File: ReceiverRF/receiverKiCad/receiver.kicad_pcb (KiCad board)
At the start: 2 copper layers, 95.4 x 60 mm, 75 parts, among them J1 RF2-03E-T-00-50-G, J2 Conn_01x05_Socket, J3 Conn_01x04, Q1 MMBT3904, SW1 SW_Push, SW2 SW_Push, SW3 SW_Push, SW4 SW_Push, SW5 SW_SPST, U1 STM32F103RET6, U2 NCV5501DT33RKG, U3 NJM2882F05-TE1, U4 MLX90393SLW-ABA-011-RE, Y1 YG8M000000S418

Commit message: changement cristal
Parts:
- Y1: value YG8M000000S418 -> CTX853CT-ND
- moved CSTL_C1 0.93 mm to (145.8, 83.2), turned to 0 degrees
- moved Y1 0.25 mm to (140.0, 84.4), turned to 0 degrees
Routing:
- net OSC_IN: track 10.2 -> 16.2 mm

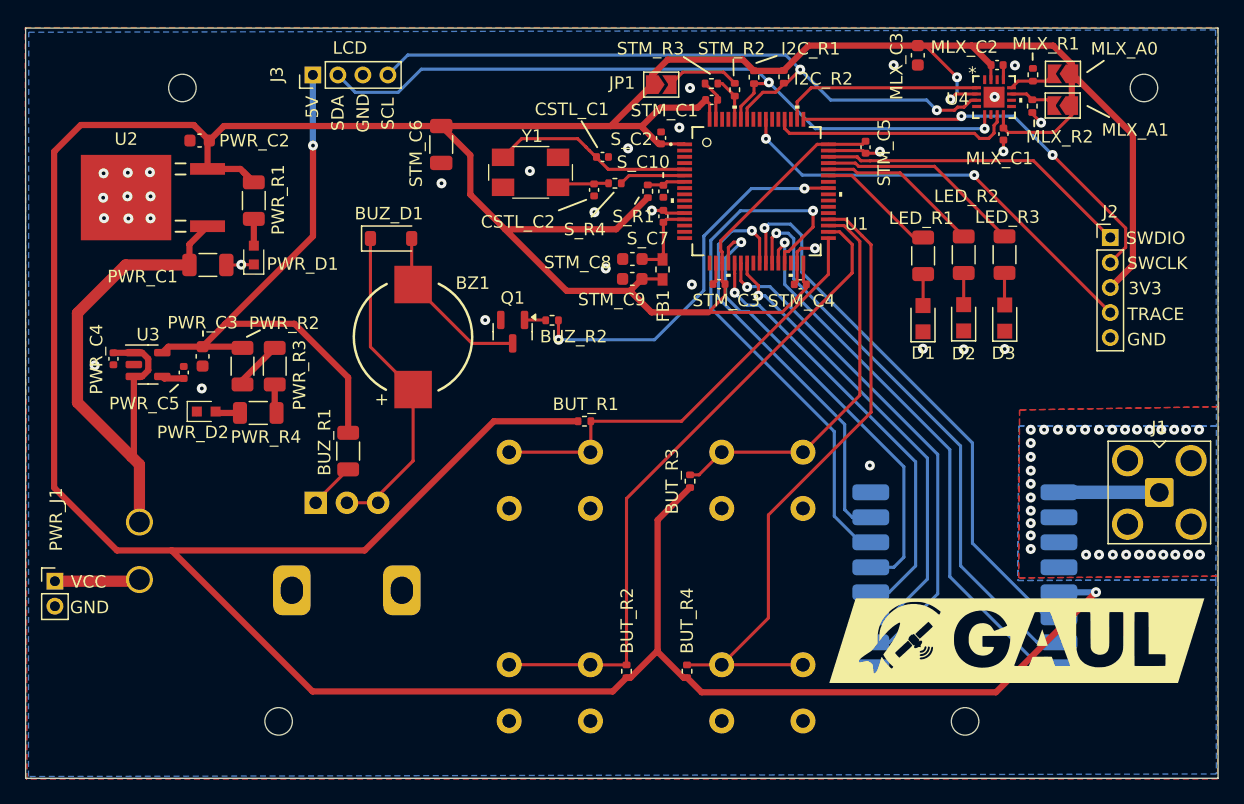
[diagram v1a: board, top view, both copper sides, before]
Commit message: changement vers footprint 1206
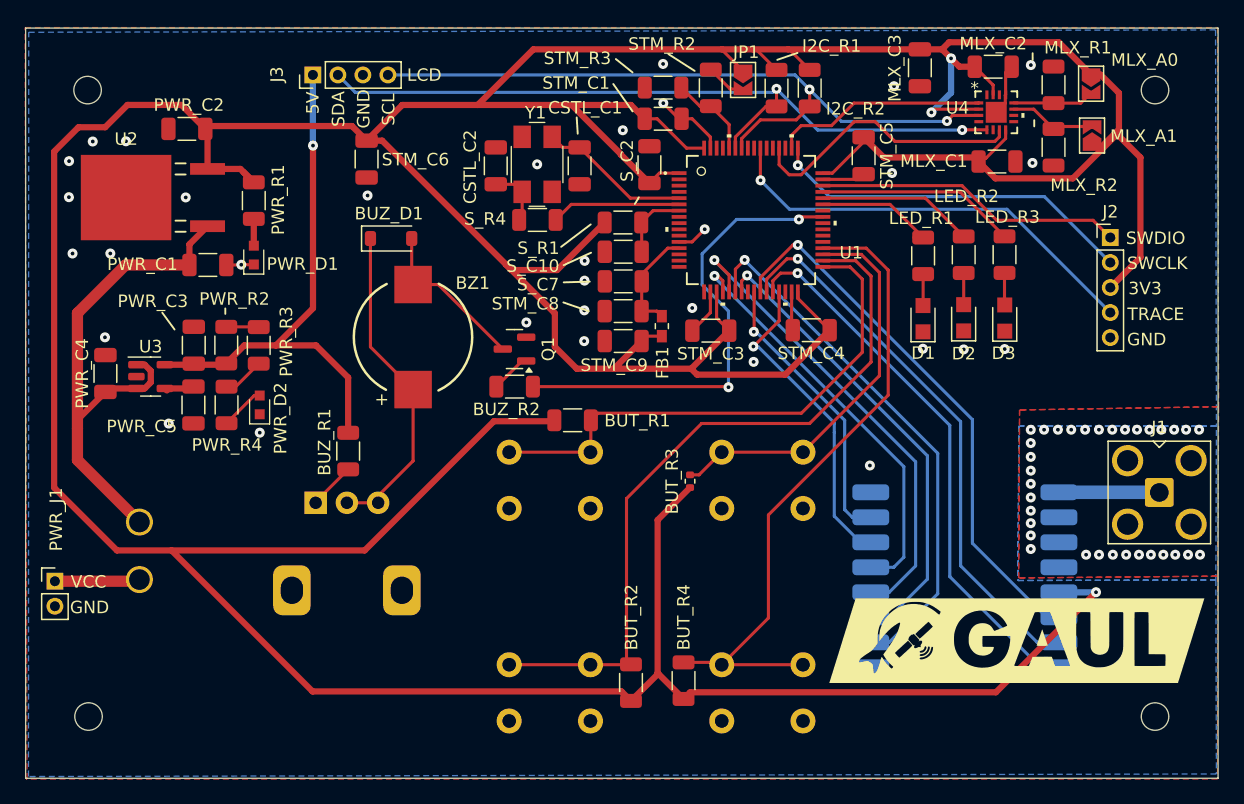
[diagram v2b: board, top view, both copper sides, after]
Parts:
- BUT_R1, BUT_R2, BUT_R4, BUZ_R2, I2C_R1, I2C_R2, MLX_R1, MLX_R2, STM_R2, STM_R3, S_R1, S_R4: footprint Resistor_SMD:R_0402_1005Metric -> Resistor_SMD:R_1206_3216Metric
- CSTL_C1, CSTL_C2, MLX_C1, MLX_C2, PWR_C4, PWR_C5, STM_C1, STM_C3, STM_C4, STM_C5, S_C10, S_C2, S_C7: footprint Capacitor_SMD:C_0402_1005Metric -> Capacitor_SMD:C_1206_3216Metric
- MLX_C3, PWR_C2, PWR_C3, STM_C8, STM_C9: footprint Capacitor_SMD:C_0603_1608Metric -> Capacitor_SMD:C_1206_3216Metric
- moved REF** 15.2 mm to (104.7, 127.9)
- moved REF** 15.2 mm to (190.0, 127.9)
- moved CSTL_C2 8.10 mm to (137.3, 83.9), turned to 90 degrees
- moved REF** 7.59 mm to (104.6, 77.8)
- moved S_R4 6.86 mm to (140.6, 88.2)
- moved JP1 6.55 mm to (157.0, 77.0), turned to -90 degrees
- moved S_C7 6.11 mm to (147.5, 93.1), turned to 180 degrees
- moved BUZ_R2 6.09 mm to (138.8, 101.5)
- moved STM_C6 6.08 mm to (126.9, 83.3)
- moved S_C10 5.80 mm to (147.5, 90.7), turned to 180 degrees
- moved STM_C9 5.02 mm to (147.5, 97.9)
- moved FB1 4.54 mm to (150.5, 96.7)
- moved PWR_D2 4.31 mm to (118.4, 103.0), turned to 90 degrees
- moved STM_C8 4.24 mm to (147.4, 95.5)
- moved STM_C1 4.16 mm to (150.6, 80.1)
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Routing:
- net +3.3V: track 406.6 -> 458.3 mm
- net RFM_NIRQ: track 44.4 -> 25.5 mm
- net RFM_SDN: track 33.7 -> 22.9 mm
- net BUZZER: track 30.8 -> 38.1 mm
- net PUSH_1: track 35.8 -> 42.6 mm
- net PUSH_2: track 52.8 -> 58.4 mm
- net OSC_OUT: track 5.32 -> 10.4 mm
- net +5V: track 48.1 -> 43.7 mm
- net OSC_IN: track 16.2 -> 12.2 mm
- net SPI_RFM_CS: track 37.4 -> 33.5 mm
- net SPI_SCK: track 35.2 -> 38.6 mm
- net BOOT0: track 3.64 -> 6.93 mm
- net SYS_SWCLK: track 32.9 -> 29.6 mm, vias 2 -> 1
- net Net-(MLX_A1-B): track 3.76 -> 7.00 mm
- net Net-(MLX_A0-B): track 3.85 -> 6.85 mm
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
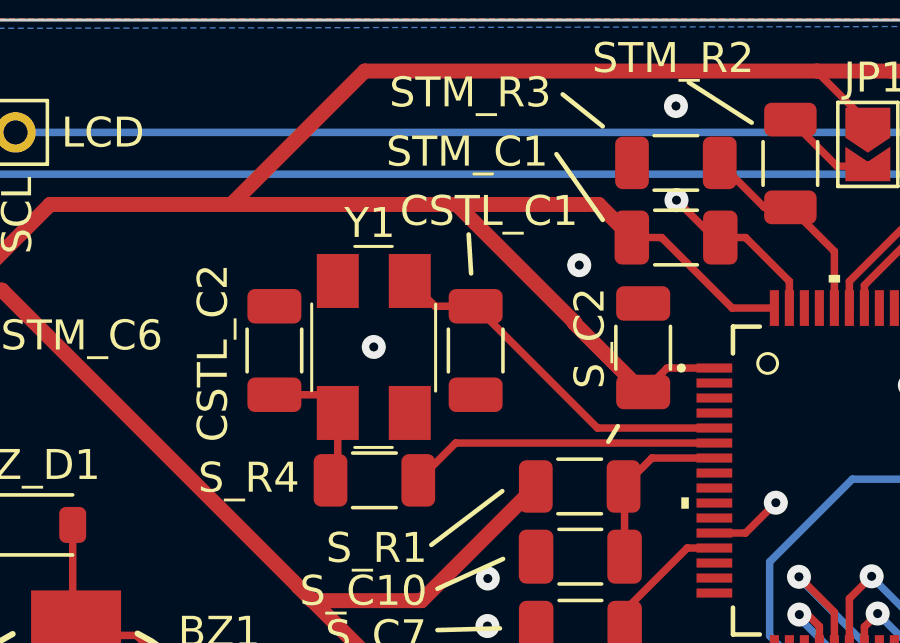
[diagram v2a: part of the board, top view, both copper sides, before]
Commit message: changement BOM et choix nouvelles pièces 1206
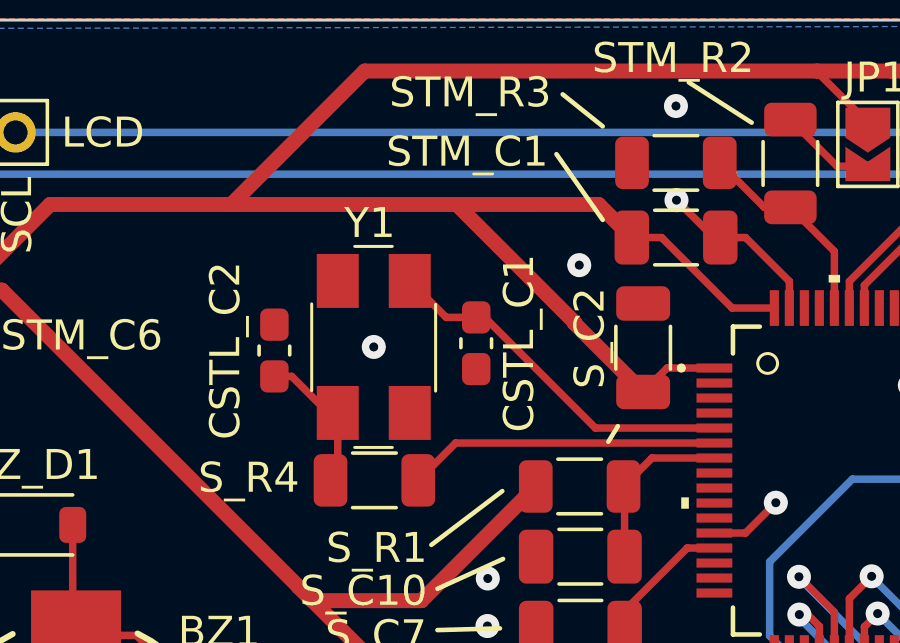
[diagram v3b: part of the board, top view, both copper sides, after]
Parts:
- CSTL_C1, CSTL_C2: footprint Capacitor_SMD:C_1206_3216Metric -> Capacitor_SMD:C_0603_1608Metric_Pad1.08x0.95mm_HandSolder
- moved CSTL_C1 0.24 mm to (144.0, 83.6)

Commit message: Ajout date, nom et version
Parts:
- IdéFIX le GAULois: renamed from Idéfix le GAULois
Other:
- board text added: "IDÉFIX V1 H2025"
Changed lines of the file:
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@@
 		(tags "capacitor handsolder")
 		(property "Reference" "CSTL_C1"
-			(at 0 -1.43 270)
+			(at 0 -1.43 -90)
 			(layer "F.SilkS")
 			(effects
@@
 		(layer "B.Cu")
 		(at 149.553616 88.27172 180)
-		(property "Reference" "Idéfix le GAULois"
-			(at 22.884707 -12.896705 0)
+		(property "Reference" "IdéFIX le GAULois"
+			(at 28.553616 -1.22828 0)
 			(layer "B.SilkS")
 			(effects
 				(font
-					(size 1.5 1.5)
+					(size 2 2)
 					(thickness 0.3)
 				)
@@
 			)
 			(justify left bottom)
+		)
+	)
+	(gr_text "IDÉFIX V1\nH2025"
+		(at 165 132 0)
+		(layer "F.SilkS")
+		(effects
+			(font
+				(size 2 2)
+				(thickness 0.3)
+			)
+			(justify left bottom)

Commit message: Auto stash before checking out "origin/ODB"
nom et commande
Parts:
- moved G*** 2.25 mm to (179.0, 119.6)
- moved SW5 1.33 mm to (108.7, 111.0)
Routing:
- net VCC: track 43.1 -> 41.8 mm
- net +3.3V: track 458.3 -> 459.1 mm
- net Net-(PWR_J1-Pin_1): track 6.82 -> 7.35 mm
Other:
- board text added: "IDÉFIX V1 H2025 Victor Deschênes"
- board text removed: "IDÉFIX V1 H2025"
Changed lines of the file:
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@@
 	(footprint "Footprints:logo"
 		(layer "F.Cu")
-		(at 178.939303 121.842457)
+		(at 179.024569 119.594898)
 		(property "Reference" "G***"
 			(at 0 0 0)
@@
 	(footprint "Footprints:SW_1MS02Q_CNK"
 		(layer "B.Cu")
-		(at 108.76054 112.361013 180)
+		(at 108.739387 111.027916 180)
 		(tags "L101011MS02Q ")
 		(property "Reference" "SW5"
@@
 		)
 	)
-	(gr_text "IDÉFIX V1\nH2025"
-		(at 165 132 0)
+	(gr_text "IDÉFIX V1\nH2025\nVictor Deschênes"
+		(at 164.287926 131.86912 0)
 		(layer "F.SilkS")
 		(effects
 			(font
-				(size 2 2)
-				(thickness 0.3)
+				(size 1.8 1.8)
+				(thickness 0.28)
 			)
 			(justify left bottom)
@@
 	)
 	(segment
-		(start 137.112385 104.296696)
-		(end 141.87046 104.296696)
-		(width 0.5)
-		(layer "F.Cu")
-		(net 6)
-	)
-	(segment
-		(start 103.886786 80.782296)
-		(end 106.021433 80.782296)
-		(width 0.5)
-		(layer "F.Cu")
-		(net 6)
-	)
-	(segment
 		(start 148.077719 126.665426)
 		(end 150.258199 124.484946)
@@
 	)
 	(segment
-		(start 107.80685 78.996879)
-		(end 112.115983 78.996879)
-		(width 0.5)
-		(layer "F.Cu")
-		(net 6)
-	)
-	(segment
-		(start 112.115983 78.996879)
-		(end 114.031406 80.912302)
-		(width 0.5)
-		(layer "F.Cu")
-		(net 6)
-	)
-	(segment
 		(start 175.892863 83.258713)
 		(end 176.467863 83.258713)
@@
 	)
 	(segment
+		(start 106.021433 80.782296)
+		(end 107.80685 78.996879)
+		(width 0.5)
+		(layer "F.Cu")
+		(net 6)
+	)
+	(segment
 		(start 160.652825 74.552072)
 		(end 171.18376 74.552072)
@@
 	)
 	(segment
-		(start 111.328411 114.629079)
-		(end 106.960546 114.629079)
-		(width 0.5)
-		(layer "F.Cu")
-		(net 6)
-	)
-	(segment
 		(start 171.18376 74.552072)
 		(end 172.957388 74.552072)
@@
 	)
 	(segment
+		(start 105.598425 113.266958)
+		(end 101.938385 109.606918)
+		(width 0.5)
+		(layer "F.Cu")
+		(net 6)
+	)
+	(segment
 		(start 116.836875 84.11638)
 		(end 117.907483 85.186988)
@@
 	)
 	(segment
-		(start 111.328411 114.629079)
-		(end 126.780002 114.629079)
-		(width 0.5)
-		(layer "F.Cu")
-		(net 6)
-	)
-	(segment
 		(start 135.821663 79.000238)
 		(end 129.784551 79.000238)
@@
 	)
 	(segment
+		(start 112.115983 78.996879)
+		(end 114.031406 80.912302)
+		(width 0.5)
+		(layer "F.Cu")
+		(net 6)
+	)
+	(segment
+		(start 137.112385 104.296696)
+		(end 128.139839 113.269243)
+		(width 0.5)
+		(layer "F.Cu")
+		(net 6)
+	)
+	(segment
 		(start 142.167802 92.204904)
 		(end 145.973008 88.399698)
@@
 	)
 	(segment
+		(start 107.80685 78.996879)
+		(end 112.115983 78.996879)
+		(width 0.5)
+		(layer "F.Cu")
+		(net 6)
+	)
+	(segment
 		(start 183.422256 84.869504)
 		(end 177.223418 84.869504)
@@
 	)
 	(segment
+		(start 109.96629 113.266958)
+		(end 105.598425 113.266958)
+		(width 0.5)
+		(layer "F.Cu")
+		(net 6)
+	)
+	(segment
+		(start 141.87046 104.296696)
+		(end 137.112385 104.296696)
+		(width 0.5)
+		(layer "F.Cu")
+		(net 6)
+	)
+	(segment
 		(start 150.207941 112.198084)
 		(end 150.207941 124.434688)
@@
 	)
 	(segment
-		(start 106.960546 114.629079)
-		(end 101.938385 109.606918)
+		(start 103.886786 80.782296)
+		(end 106.021433 80.782296)
 		(width 0.5)
 		(layer "F.Cu")
@@
 	)
 	(segment
-		(start 126.780002 114.629079)
-		(end 137.112385 104.296696)
+		(start 101.938385 82.730697)
+		(end 103.886786 80.782296)
 		(width 0.5)
 		(layer "F.Cu")
@@
 	)
 	(segment
+		(start 109.968575 113.269243)
+		(end 128.139839 113.269243)
+		(width 0.5)
+		(layer "F.Cu")
+		(net 6)
+	)
+	(segment
 		(start 188.825779 83.200071)
 		(end 188.825779 91.193383)
@@
 	)
 	(segment
+		(start 111.328411 114.629079)
+		(end 109.96629 113.266958)
+		(width 0.5)
+		(layer "F.Cu")
+		(net 6)
+	)
+	(segment
 		(start 187.10742 81.481712)
 		(end 188.825779 83.200071)
@@
 	)
 	(segment
-		(start 101.938385 82.730697)
-		(end 103.886786 80.782296)
-		(width 0.5)
-		(layer "F.Cu")
-		(net 6)
-	)
-	(segment
 		(start 164.189954 84.452142)
 		(end 166.684946 81.95715)
@@
 	)
 	(segment
-		(start 106.021433 80.782296)
-		(end 107.80685 78.996879)
-		(width 0.5)
-		(layer "F.Cu")
-		(net 6)
-	)
-	(segment
 		(start 152.892093 100.09589)
 		(end 153.368108 100.571905)
@@
 	)
 	(segment
-		(start 141.87046 104.296696)
-		(end 141.946682 104.220474)
-		(width 0.5)
+		(start 155.935656 97.052327)
+		(end 154.926128 96.042799)
+		(width 0.25)
 		(layer "F.Cu")
 		(net 6)
 	)
 	(segment
-		(start 155.935656 97.052327)
-		(end 154.926128 96.042799)
-		(width 0.25)
+		(start 141.946682 104.220474)
+		(end 141.87046 104.296696)
+		(width 0.5)
 		(layer "F.Cu")
 		(net 6)
@@
 	)
 	(segment
+		(start 103.80348 105.776776)
+		(end 108.739387 110.712683)
+		(width 0.9)
+		(layer "F.Cu")
+		(net 30)
+	)
+	(segment
 		(start 109.180212 101.674655)
 		(end 109.670878 101.183989)
@@
 	)
 	(segment
-		(start 103.80348 107.403953)
-		(end 108.76054 112.361013)
+		(start 103.80348 104.866415)
+		(end 103.80348 105.776776)
 		(width 0.9)
 		(layer "F.Cu")
@@
 	)
 	(segment
+		(start 108.739387 110.712683)
+		(end 108.739387 111.027916)
+		(width 0.9)
+		(layer "F.Cu")
+		(net 30)
+	)
+	(segment
 		(start 109.180212 99.774655)
 		(end 108.517713 99.774655)
@@
 	)
 	(segment
-		(start 103.80348 104.866415)
-		(end 103.80348 107.403953)
-		(width 0.9)
-		(layer "F.Cu")
-		(net 30)
-	)
-	(segment
 		(start 109.670878 100.265321)
 		(end 109.180212 99.774655)
@@
 	)
 	(segment
-		(start 108.628979 117.092575)
-		(end 108.76054 116.961014)
-		(width 0.5)
+		(start 107.274729 117.092575)
+		(end 108.739387 115.627917)
+		(width 0.9)
 		(layer "F.Cu")
 		(net 34)
@@
 	(segment
 		(start 101.999565 117.092575)
-		(end 108.628979 117.092575)
+		(end 107.274729 117.092575)
 		(width 0.9)
 		(layer "F.Cu")

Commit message: firmware oscillateur interne :(
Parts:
- BUT_R3: footprint Resistor_SMD:R_0402_1005Metric -> Resistor_SMD:R_1206_3216Metric
- moved BUT_R3 1.12 mm to (151.7, 109.3)
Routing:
- net +3.3V: track 459.1 -> 457.5 mm
- net PUSH_2: track 58.4 -> 60.0 mm
- net PUSH_3: track 31.8 -> 32.6 mm

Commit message: ideFIX v2 fix schematic, layout
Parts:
- removed the REF** at (104.7, 127.9)
- removed the REF** at (190.0, 127.9)
- removed the REF** at (190.0, 77.8)
- removed the REF** at (104.6, 77.8)
- added D4: LTST-C170GKT, Footprints:LTST-C170GKT, F.Cu at (136.3, 77.1)
- added IF1: ~, Footprints:CONN10_530481010_MOL, F.Cu at (159.0, 43.1)
- added IF2: ~, Footprints:CONN10_530481010_MOL, F.Cu at (157.4, 99.9)
- added J4: Conn_01x04, Connector_PinHeader_2.54mm:PinHeader_1x04_P2.54mm_Vertical, B.Cu at (109.7, 122.0)
- added LLS_C1: 100nF, Capacitor_SMD:C_1206_3216Metric, B.Cu at (115.1, 111.7)
- added LLS_C2: 100nF, Capacitor_SMD:C_1206_3216Metric, B.Cu at (115.2, 119.6)
- added LLS_R2: 10k, Resistor_SMD:R_1206_3216Metric, B.Cu at (115.2, 122.6)
- added PWR_R5: 100k, Resistor_SMD:R_1206_3216Metric, F.Cu at (136.3, 79.7)
- added Q2: PMOS, Footprints:SOT-23, F.Cu at (136.2, 83.8)
- added REF**: Mounting_holes, Footprints:Mounting_holes, F.Cu at (155.7, 63.9)
- added REF**: Mounting_holes_big, Footprints:Mounting_holes_big, F.Cu at (155.4, 125.7)
- added REF**: Mounting_holes, Footprints:Mounting_holes, F.Cu at (155.9, 121.3)
- added U5: TXS0102DCUR, Footprints:SOP50P310X90-8N, B.Cu at (115.1, 115.4)
- BUT_R1, BUT_R2, BUT_R3, BUT_R4, BUZ_D1, BUZ_R1, BUZ_R2, BZ1, Q1: moved to B.Cu
- D1: value LTST-C170GKT -> BZV55C18; footprint Footprints:LTST-C170GKT -> Diode_SMD:D_MiniMELF
- J2: footprint Connector_PinHeader_2.00mm:PinHeader_1x05_P2.00mm_Vertical -> Connector_PinHeader_2.54mm:PinHeader_1x05_P2.54mm_Vertical
- J3: value Conn_01x04 -> Conn_01x02_Socket; footprint Connector_PinHeader_2.00mm:PinHeader_1x04_P2.00mm_Vertical -> Connector_PinHeader_2.54mm:PinHeader_1x02_P2.54mm_Vertical
- PWR_J1: footprint Connector_PinHeader_2.00mm:PinHeader_1x02_P2.00mm_Vertical -> Connector_PinHeader_2.54mm:PinHeader_1x02_P2.54mm_Vertical
- RF1: footprint Footprints:RFM22b-S2 -> Footprints:RFM22b-S2_TH
- RV1, SW1, SW2, SW3, SW4: moved to F.Cu
- SW5: value SW_SPST -> SW_SPDT; footprint Footprints:SW_1MS02Q_CNK -> Footprints:CS12ANW03_NKK; moved to F.Cu
- moved G*** 140.9 mm to (115.4, 245.3)
- moved BUZ_D1 81.4 mm to (187.5, 146.1), turned to 180 degrees
- moved BZ1 77.8 mm to (196.3, 139.3), turned to 180 degrees
- moved RV1 75.8 mm to (198.3, 118.4)
- moved BUZ_R1 71.8 mm to (196.7, 115.4), turned to 180 degrees
- moved J3 63.7 mm to (175.4, 40.9), turned to -90 degrees
- moved PWR_D2 63.5 mm to (147.4, 46.5)
- moved PWR_C4 63.5 mm to (135.0, 44.0)
- moved PWR_C5 63.5 mm to (142.1, 46.5)
- moved PWR_C3 63.5 mm to (142.1, 41.7)
- moved PWR_R2 63.5 mm to (144.7, 41.7)
- moved PWR_R4 63.5 mm to (144.7, 46.5)
- moved U3 63.5 mm to (138.6, 44.2)
- moved PWR_R3 63.5 mm to (147.3, 41.7)
- moved IdéFIX le GAULois 63.4 mm to (96.3, 53.8)
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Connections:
- BUT_R1 pad 1: +3.3V -> +3.3V_IB
- BUT_R1 pad 2: PUSH_1 -> PUSH_1_IB
- BUT_R2 pad 1: +3.3V -> +3.3V_IB
- BUT_R2 pad 2: PUSH_2 -> PUSH_2_IB
- BUT_R3 pad 1: +3.3V -> +3.3V_IB
- BUT_R3 pad 2: PUSH_3 -> PUSH_3_IB
- BUT_R4 pad 1: +3.3V -> +3.3V_IB
- BUT_R4 pad 2: PUSH_4 -> PUSH_4_IB
- BUZ_R1 pad 2: +5V -> +5V_IB
- BUZ_R2 pad 1: BUZZER -> BUZZER_IB
- D1 pad 1: GND -> VCC
- J3 pad 1: +5V -> UART4_TX
- J3 pad 2: I2C_SDA -> UART4_RX
- LED_R1 pad 2: Net-(D1-A) -> Net-(D2-A)
- LED_R2 pad 2: Net-(D2-A) -> Net-(D3-A)
- LED_R3 pad 2: Net-(D3-A) -> Net-(D4-A)
- Q1 pad 3: GND -> GND_IB
- RF1 pad 3: unconnected-(RF1-RX_ANT-Pad3) -> RFM_GPIO4
- RF1 pad 4: unconnected-(RF1-TX_ANT-Pad4) -> RFM_GPIO5
- SW1 pad 1: PUSH_1 -> PUSH_1_IB
- SW1 pad 2: GND -> GND_IB
- SW2 pad 1: PUSH_2 -> PUSH_2_IB
- SW2 pad 2: GND -> GND_IB
- SW3 pad 1: PUSH_3 -> PUSH_3_IB
- SW3 pad 2: GND -> GND_IB
- SW4 pad 1: PUSH_4 -> PUSH_4_IB
- SW4 pad 2: GND -> GND_IB
- SW5 pad 1: VCC -> Net-(Q2-D)
- U1 pad 14: unconnected-(U1-PA0-Pad14) -> LED1
- U1 pad 15: unconnected-(U1-PA1-Pad15) -> LED2
- U1 pad 16: unconnected-(U1-PA2-Pad16) -> LED3
- U1 pad 17: unconnected-(U1-PA3-Pad17) -> RFM_SDN
- U1 pad 20: SPI_RFM_CS -> RFM_NIRQ
- U1 pad 24: unconnected-(U1-PC4-Pad24) -> SPI_RFM_CS
- U1 pad 25: RFM_SDN -> RFM_GPIO3
- U1 pad 26: RFM_GPIO1 -> RFM_GPIO2
- U1 pad 27: RFM_GPIO2 -> RFM_GPIO1
- U1 pad 28: RFM_GPIO3 -> RFM_GPIO5
- U1 pad 29: RFM_NIRQ -> RFM_GPIO4
- U1 pad 33: PUSH_1 -> unconnected-(U1-PB12-Pad33)
- U1 pad 34: PUSH_2 -> unconnected-(U1-PB13-Pad34)
- U1 pad 35: PUSH_3 -> unconnected-(U1-PB14-Pad35)
- U1 pad 36: PUSH_4 -> unconnected-(U1-PB15-Pad36)
- U1 pad 37: unconnected-(U1-PC6-Pad37) -> PUSH_1
- U1 pad 38: unconnected-(U1-PC7-Pad38) -> PUSH_2
- U1 pad 39: unconnected-(U1-PC8-Pad39) -> PUSH_3
- U1 pad 40: unconnected-(U1-PC9-Pad40) -> PUSH_4
- U1 pad 41: BUZZER -> unconnected-(U1-PA8-Pad41)
- U1 pad 43: LED1 -> BUZZER
- U1 pad 44: LED2 -> MLX_INT
- U1 pad 45: LED3 -> MLX_INT/TRIG
- U1 pad 50: MLX_INT -> unconnected-(U1-PA15-Pad50)
- U1 pad 51: unconnected-(U1-PC10-Pad51) -> UART4_TX
- U1 pad 52: MLX_INT/TRIG -> UART4_RX
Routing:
- net +3.3V: track 457.5 -> 0.00 mm, vias 3 -> 0
- net I2C_SDA: track 60.6 -> 0.00 mm, vias 2 -> 0
- net PUSH_2: track 60.0 -> 0.00 mm
- net I2C_SCL: track 57.6 -> 0.00 mm, vias 2 -> 0
- net PUSH_4: track 52.7 -> 0.00 mm
- net RFM_GPIO2: track 44.5 -> 0.00 mm, vias 1 -> 0
- net RFM_GPIO1: track 44.2 -> 0.00 mm, vias 1 -> 0
- net RFM_GPIO3: track 44.2 -> 0.00 mm, vias 1 -> 0
- net +5V: track 43.7 -> 0.00 mm, vias 1 -> 0
- net SPI_MISO: track 42.9 -> 0.00 mm, vias 1 -> 0
- net PUSH_1: track 42.6 -> 0.00 mm
- net VCC: track 41.8 -> 0.00 mm
- net SPI_SCK: track 38.6 -> 0.00 mm, vias 1 -> 0
- net BUZZER: track 38.1 -> 0.00 mm, vias 2 -> 0
- net SPI_MOSI: track 37.6 -> 0.00 mm, vias 1 -> 0
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- removed copper zone on B.Cu, net GND
- removed copper zone on F.Cu, net GND
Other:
- board size 95.4 x 60 mm -> 100 x 116.6 mm
